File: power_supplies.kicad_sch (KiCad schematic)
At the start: 44 parts, among them IC4 MCP1792T-5002H_CB, IC5 MCP1792T-5002H_CB, J3 12V supply, J5 490107670612, Q3 2N7002BK,215, Q4 Si2333DS, Q5 2N7002BK,215, T1 760390014, U1 PIC10F322-IOT

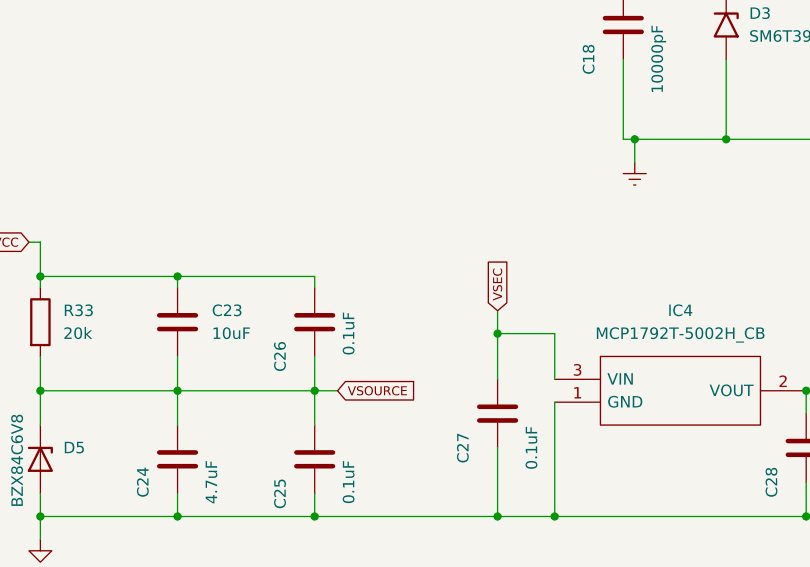
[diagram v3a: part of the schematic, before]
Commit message: Design with footprint error
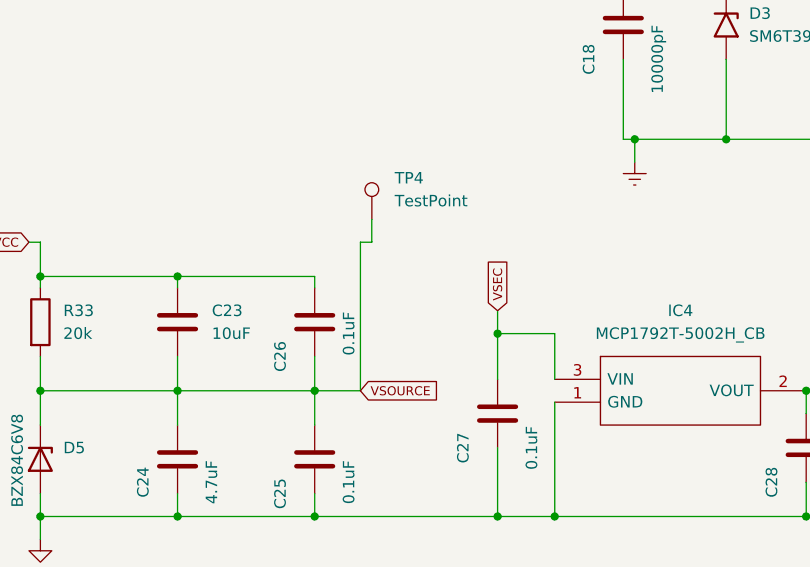
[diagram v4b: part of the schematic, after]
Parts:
- added TP4: TestPoint, TestPoint:TestPoint_Pad_D1.0mm, symbol Connector:TestPoint
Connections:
- net VSOURCE: now also TP4.1
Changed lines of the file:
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@@
+    (stroke (width 0) (type default))
+  )
+  (wire (pts (xy 69.85 153.67) (xy 68.58 153.67))
     (stroke (width 0) (type default))
   )
@@
     (stroke (width 0) (type default))
   )
-  (wire (pts (xy 66.04 170.18) (xy 63.5 170.18))
-    (stroke (width 0) (type default))
-  )
   (wire (pts (xy 33.02 52.07) (xy 35.56 52.07))
     (stroke (width 0) (type default))
@@
     (stroke (width 0) (type default))
   )
+  (wire (pts (xy 63.5 170.18) (xy 68.58 170.18))
+    (stroke (width 0) (type default))
+  )
   (wire (pts (xy 67.31 74.93) (xy 76.2 74.93))
     (stroke (width 0) (type default))
@@
   )
   (wire (pts (xy 67.31 69.85) (xy 115.57 69.85))
+    (stroke (width 0) (type default))
+  )
+  (wire (pts (xy 68.58 153.67) (xy 68.58 170.18))
+    (stroke (width 0) (type default))
+  )
+  (wire (pts (xy 69.85 151.13) (xy 69.85 153.67))
     (stroke (width 0) (type default))
   )
@@
     )
   )
-  (global_label "VSOURCE" (shape input) (at 66.04 170.18 0) (fields_autoplaced)
+  (global_label "VSOURCE" (shape input) (at 68.58 170.18 0) (fields_autoplaced)
     (effects (font (size 1 1) (color 115 71 255 1)) (justify left))
-    (property "Intersheetrefs" "${INTERSHEET_REFS}" (at 75.1998 170.18 0)
+    (property "Intersheetrefs" "${INTERSHEET_REFS}" (at 77.7398 170.18 0)
       (effects (font (size 1.27 1.27)) (justify left) hide)
     )
@@
         )
       )
+    )
+  )
+  (symbol (lib_id "Connector:TestPoint") (at 69.85 151.13 0) (unit 1)
+    (in_bom yes) (on_board yes) (dnp no) (fields_autoplaced)
+    (property "Reference" "TP4" (at 72.39 146.558 0)
+      (effects (font (size 1.27 1.27)) (justify left))
+    )
+    (property "Value" "TestPoint" (at 72.39 149.098 0)
+      (effects (font (size 1.27 1.27)) (justify left))
+    )
+    (property "Footprint" "TestPoint:TestPoint_Pad_D1.0mm" (at 74.93 151.13 0)
+      (effects (font (size 1.27 1.27)) hide)
+    )
+    (property "Datasheet" "~" (at 74.93 151.13 0)
+      (effects (font (size 1.27 1.27)) hide)
+    )
+    (pin "1")
+    (instances
+      (project "SiC based Battery Disconnect"
+        (path "/525387b1-1528-4728-a616-6f57d2a34d69/925d75c4-de6e-4540-9e02-6341c2b379d1"
+          (reference "TP4") (unit 1)
+        )
+      )

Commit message: Final Design
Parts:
- D3: value SM6T39A -> SM6T68CA
- J3: value 12V supply -> 12V/48V supply
- R33: value 20k -> 4.7k
- TP9: value 5001 -> 5001/TestPoint
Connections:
- net Earth: now also C17.2; no longer C17.1
- net VDDLV: now also C17.1; no longer C17.2
- net RA0_{lv}: now reaches J5.4, Q3.1 (G), R4.1, U1.1 (RA0)
- net RA1_{lv}: now reaches J5.5, Q5.1 (G), R7.1, U1.3 (RA1)
- net RA3_{lv}: now reaches J5.1, R8.2, U1.6 (RA3)
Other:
- moved on the sheet: C17, C18, C19, C20, C21, C22, C23, C24, C25, C26, C27, C28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
